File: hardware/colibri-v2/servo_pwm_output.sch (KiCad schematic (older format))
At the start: 15 parts

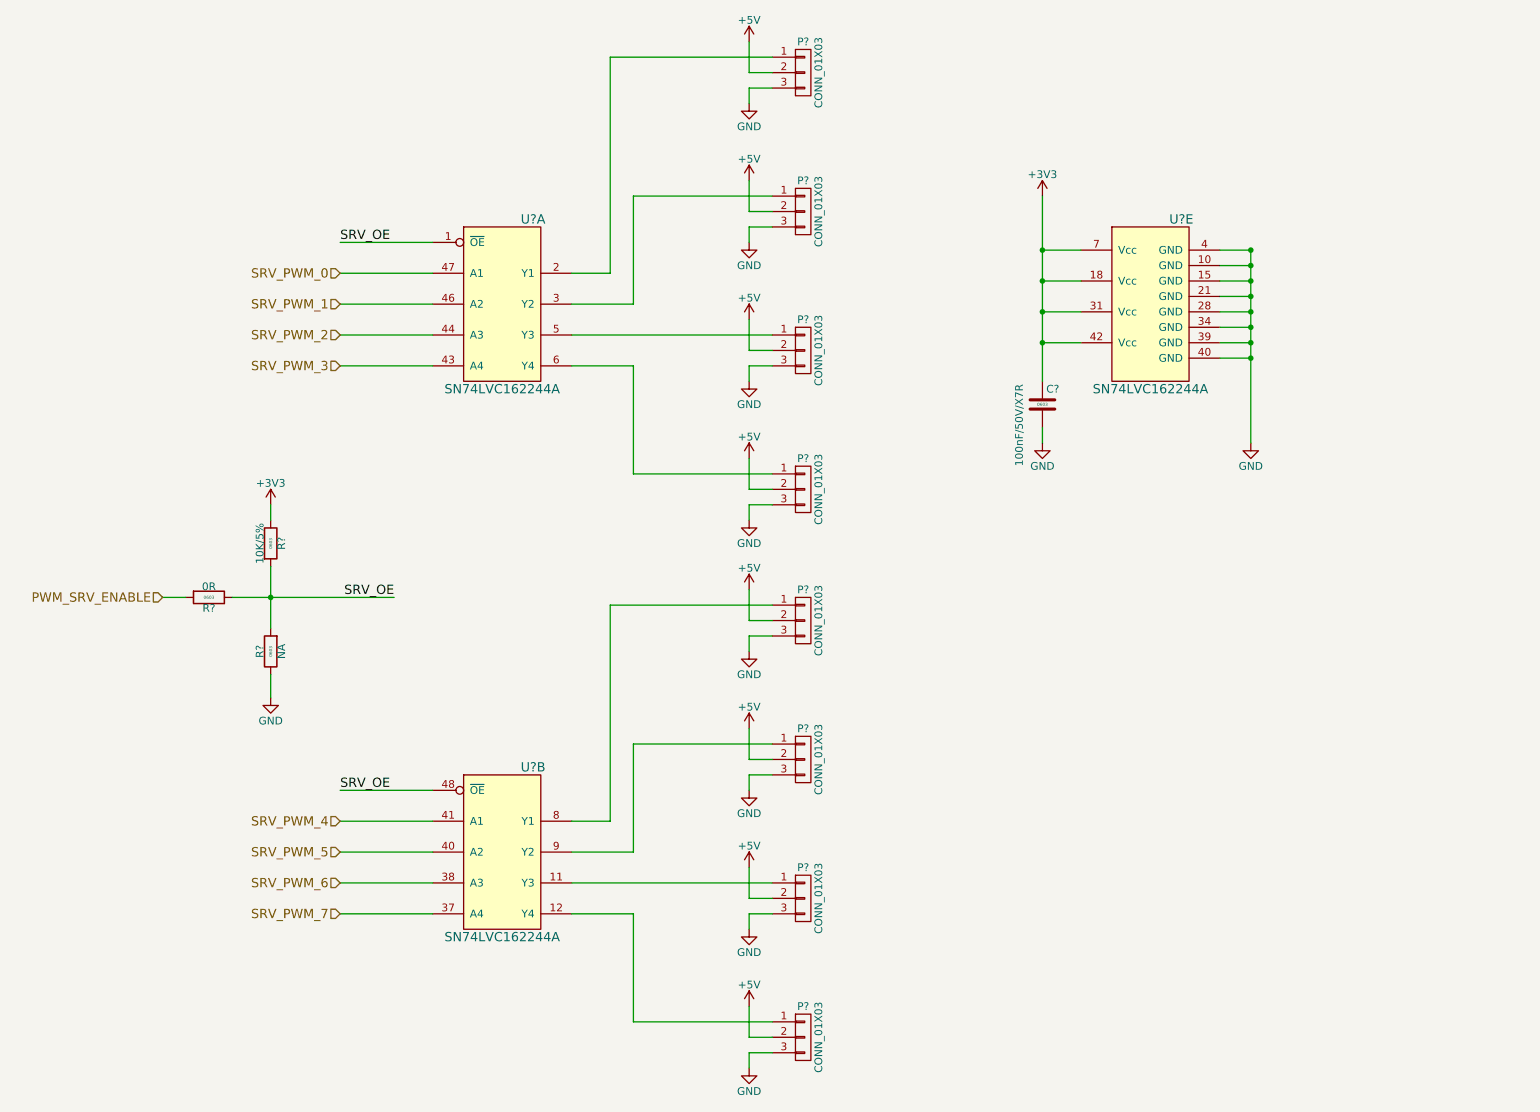
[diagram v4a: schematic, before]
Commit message: Added Power-On-Reset controller MCP120 to the Cortex
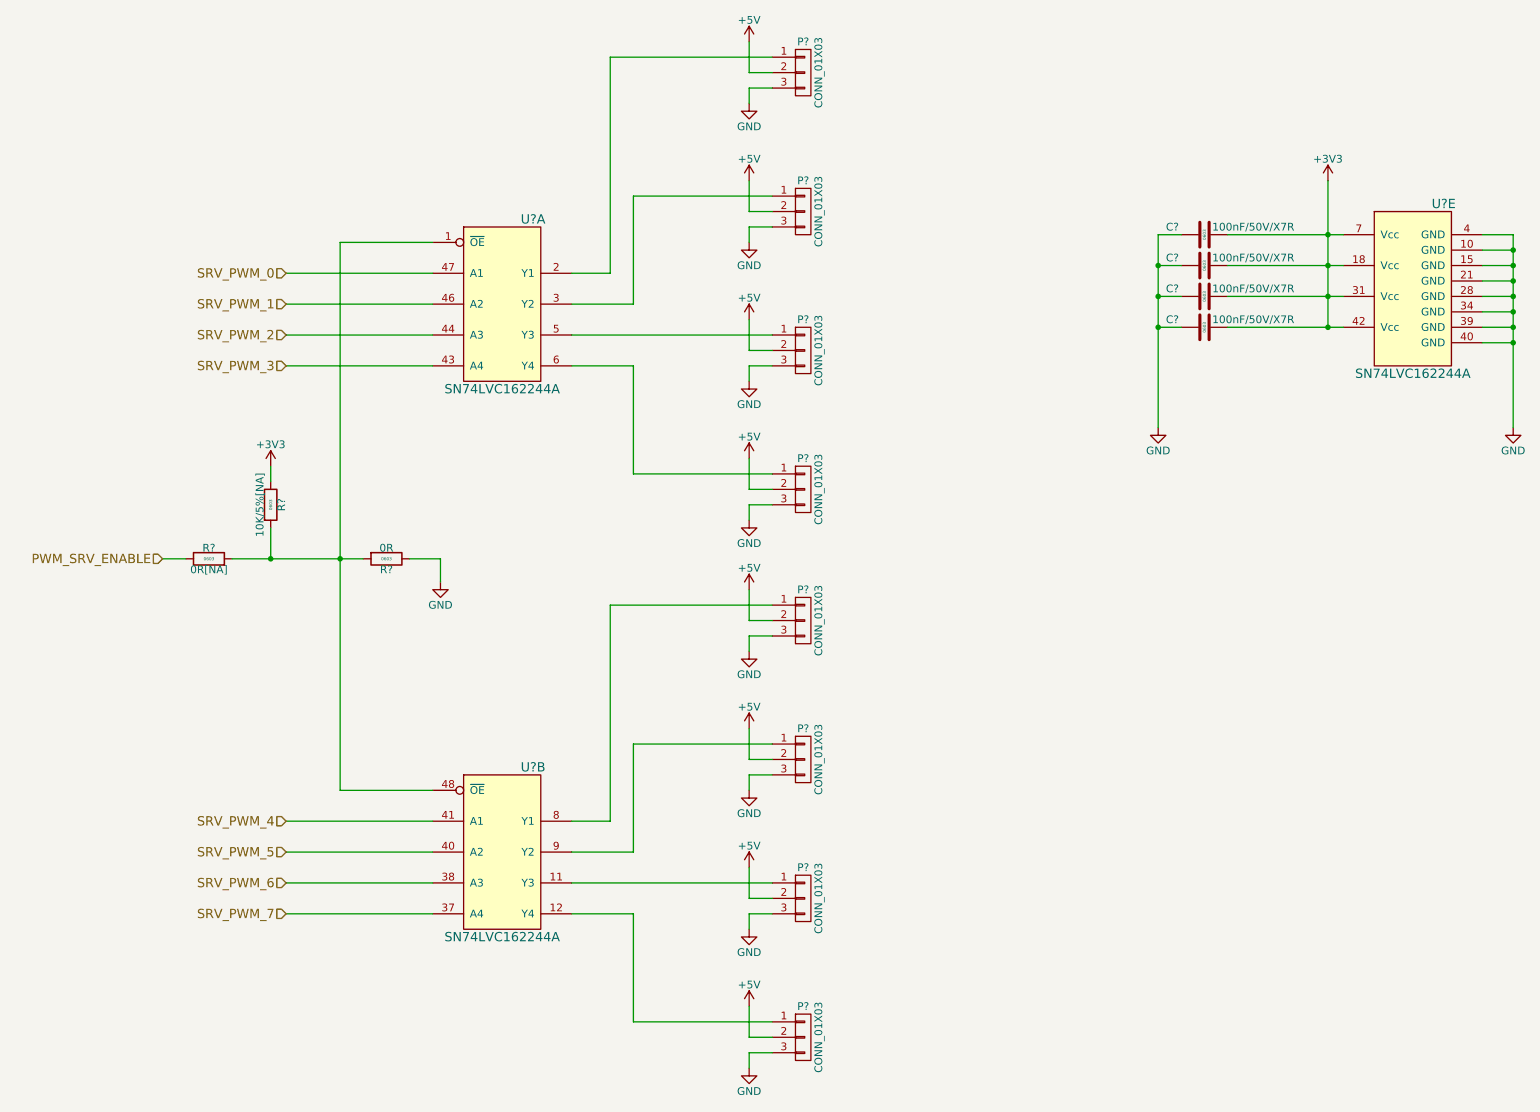
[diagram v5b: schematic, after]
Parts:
- removed C?: 100nF/50V/X7R, Capacitors_SMD:C_0603, symbol C_SMT
- added C? (x4): 100nF/50V/X7R, Capacitors_SMD:C_0603, symbol C_SMT
- R?: value 10K/5% -> 10K/5%[NA]
- R?: value NA -> 0R[NA]
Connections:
- net +3V3: now also C?.1, C?.1, C?.1, C?.1
- net GND: now also R?.1, C?.2, C?.2, C?.2, C?.2; no longer R?.1
- net PWM_SRV_ENABLE: now also R?.1; no longer R?.2
- net SRV_OE: no longer names the net of R?.2, R?.2, U?.1 (~OE), U?.48 (~OE)
- net SRV_OE: now also R?.2; no longer R?.1
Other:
- moved on the sheet: R?, U?E
